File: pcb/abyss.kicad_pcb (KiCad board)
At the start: 2 copper layers, 106.5 x 91.8 mm, 37 parts

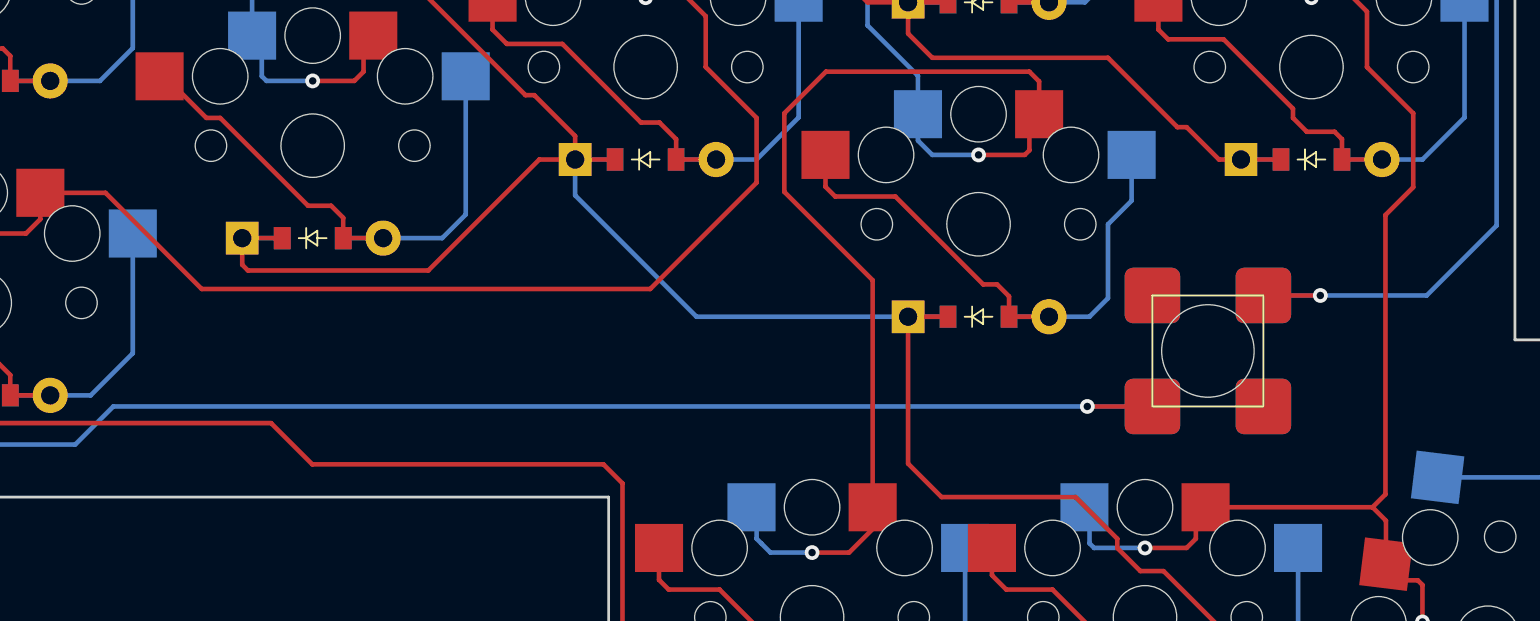
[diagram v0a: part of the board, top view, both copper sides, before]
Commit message: Fix rst btn
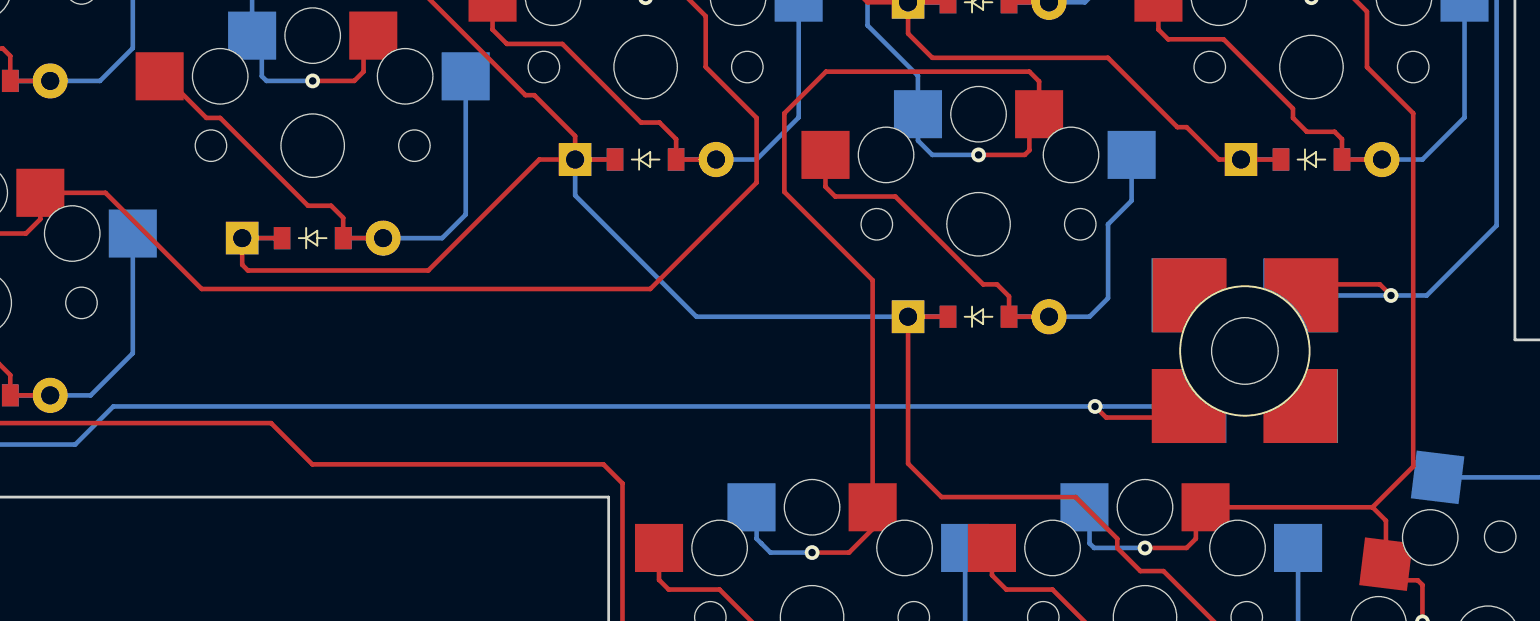
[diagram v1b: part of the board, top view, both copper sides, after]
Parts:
- moved REF** 2.00 mm to (168.4, 102.6)
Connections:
- REF** pad 1: GND -> (no net)
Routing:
- net RST: track 148.0 -> 150.5 mm
- net GND: track 215.5 -> 214.5 mm

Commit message: wip: Battery and mc fixes
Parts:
- removed JST1: , ceoloide/battery_connector_jst_ph_2
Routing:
- net GND: track 214.5 -> 177.2 mm, vias 4 -> 3
- net BAT_P: track 101.0 -> 86.3 mm, vias 2 -> 1
- net JST1_2: track 3.60 -> 0.00 mm
- net JST1_1: track 3.60 -> 0.00 mm
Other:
- board text added: "RST"

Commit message: wip: Battery and mc fixes
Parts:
- added REF**: CONN_SM02B-SRSS-TB_JST, Library:CONN_SM02B-SRSS-TB_JST, F.Cu at (171.0, 53.7)
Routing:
- net GND: track 177.2 -> 201.2 mm, vias 3 -> 4
- net BAT_P: track 86.3 -> 99.8 mm, vias 1 -> 2

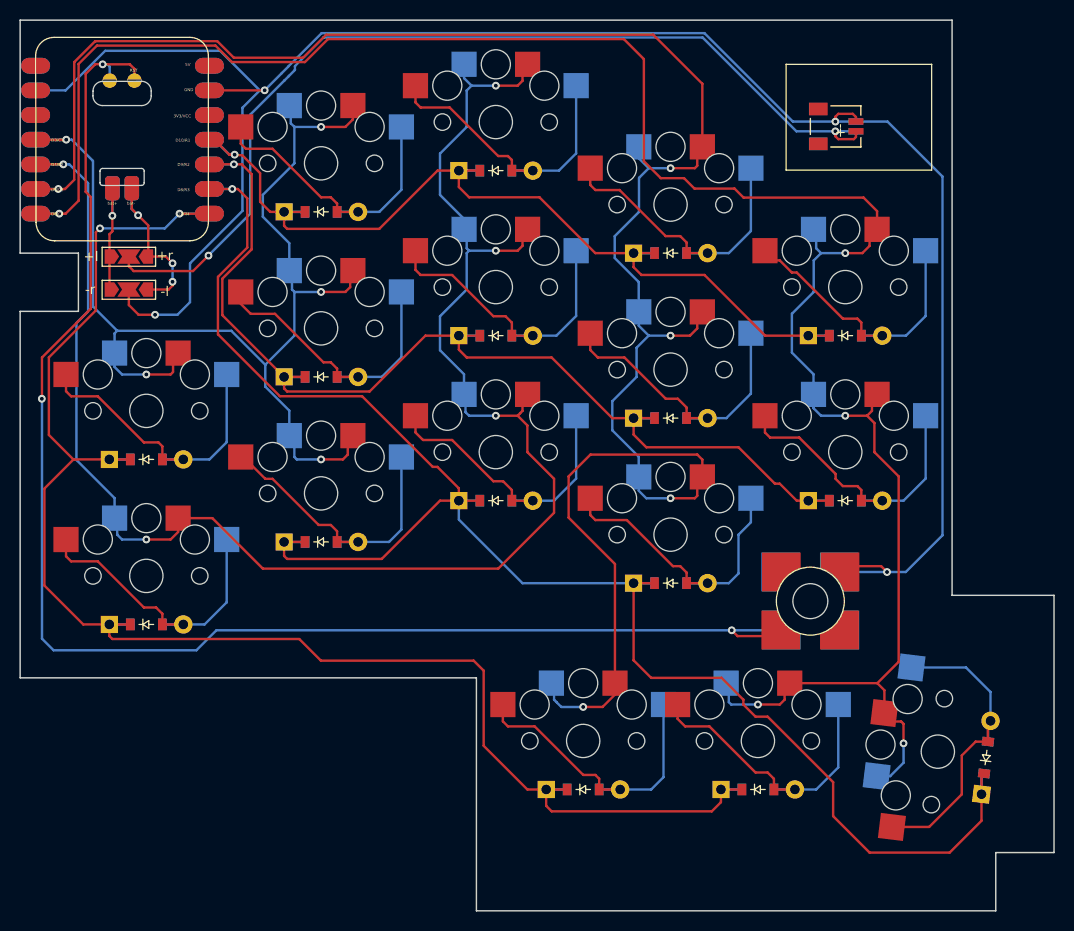
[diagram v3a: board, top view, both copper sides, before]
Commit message: Add pcb tri jumper for reset
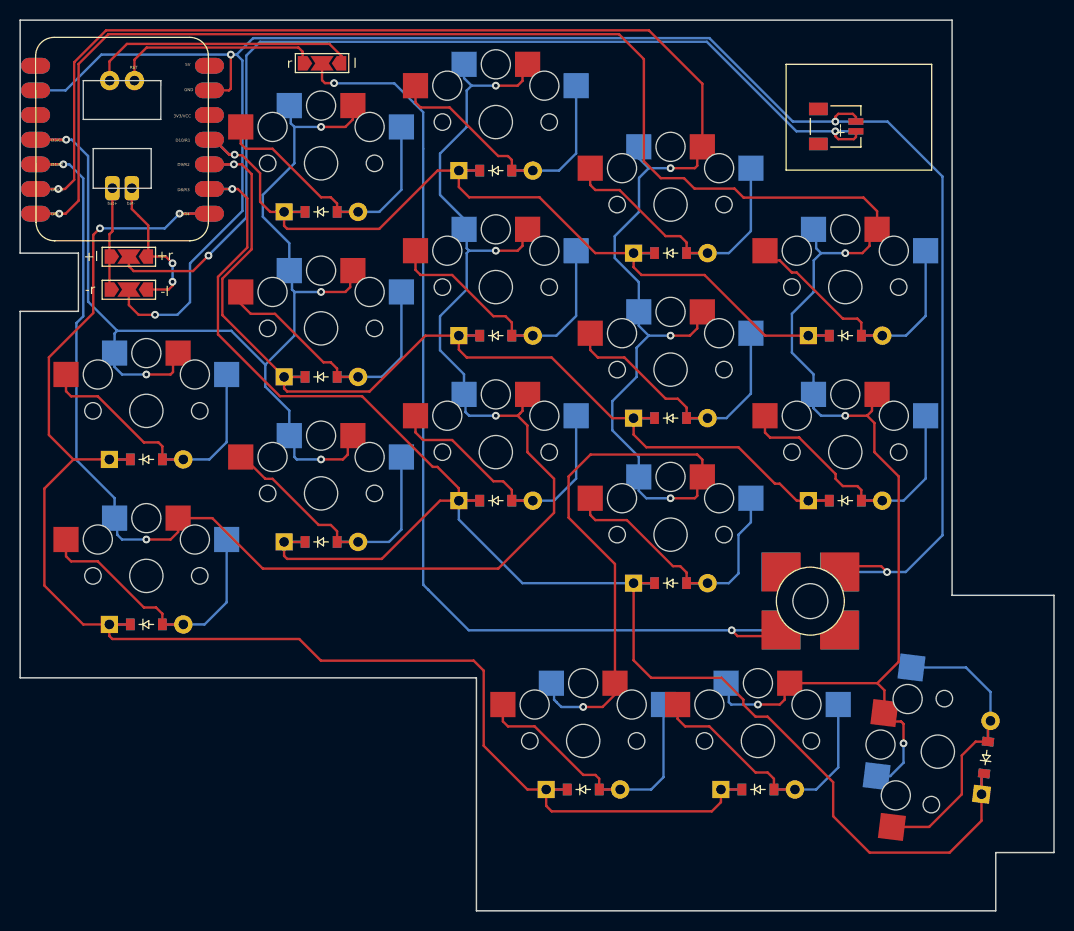
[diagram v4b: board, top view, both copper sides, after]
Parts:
- added REF**: SolderJumper-3_P2.0mm_Open_TrianglePad1.0x1.5mm_NumberLabels, Jumper:SolderJumper-3_P2.0mm_Open_TrianglePad1.0x1.5mm_NumberLabels, F.Cu at (118.1, 47.2)
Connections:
- REF** pad 16: bat_right -> bat_left
- REF** pad 17: RST -> RST_R
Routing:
- net RST: track 150.5 -> 105.2 mm, vias 3 -> 2
- net RST_L: track 0.00 -> 27.5 mm
- net RST_R: track 0.00 -> 21.0 mm
- net BAT_P: track 99.8 -> 103.0 mm
- net bat_right: track 18.4 -> 15.5 mm, vias 3 -> 2
- net bat_left: track 13.3 -> 10.6 mm, vias 1 -> 0
- net C3: track 209.4 -> 208.3 mm
- net C4: track 220.4 -> 219.4 mm
- net GND: track 201.2 -> 200.7 mm
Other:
- board text removed: "RST"

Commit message: Fix resetbtn & bat conn
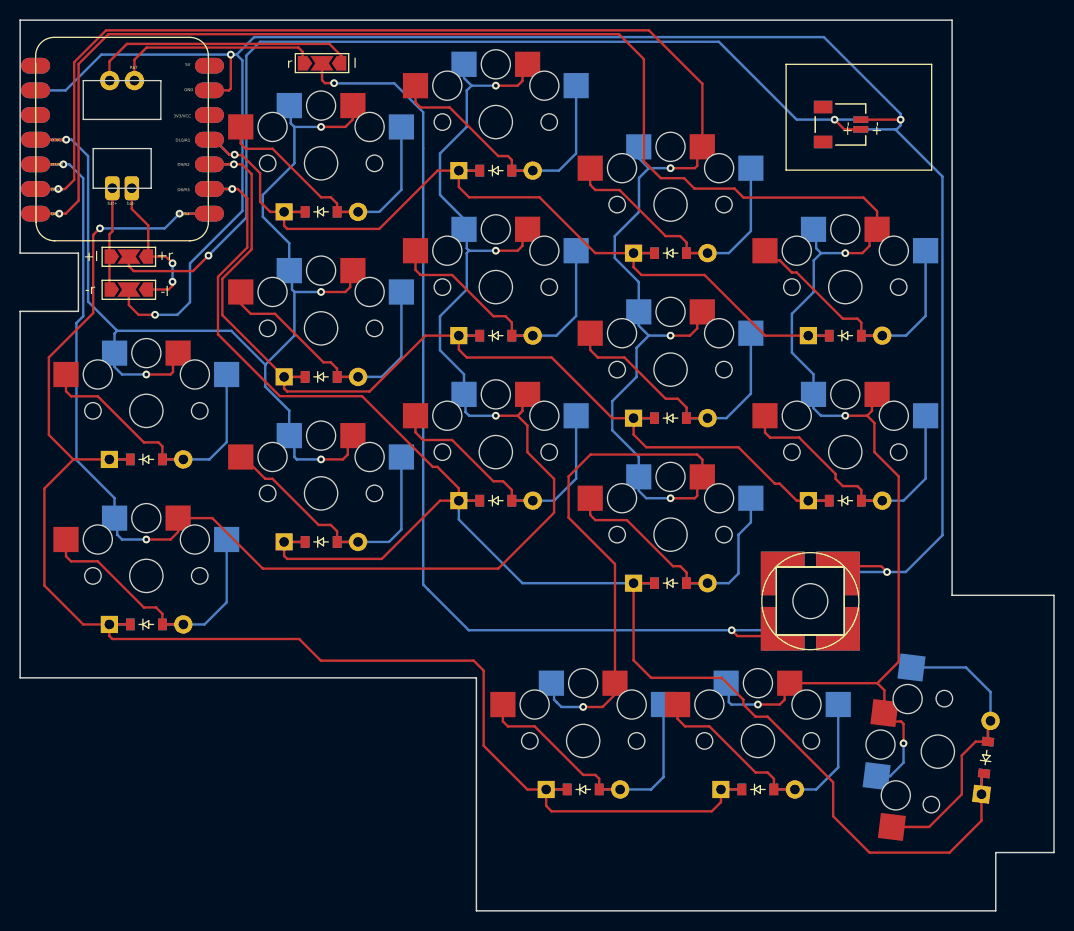
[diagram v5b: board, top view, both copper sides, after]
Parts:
- moved REF** 0.54 mm to (171.5, 53.5)
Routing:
- net GND: track 200.7 -> 206.9 mm
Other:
- board text added: "+"
- board text added: "-"
